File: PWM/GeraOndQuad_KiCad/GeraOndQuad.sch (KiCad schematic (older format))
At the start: 54 parts, among them J1 Conn_01x04_Female, J2 Conn_01x02_Female, J3 Conn_01x02_Female, U1 LM324, U2 TL494, U3 LM324, U4 TL494

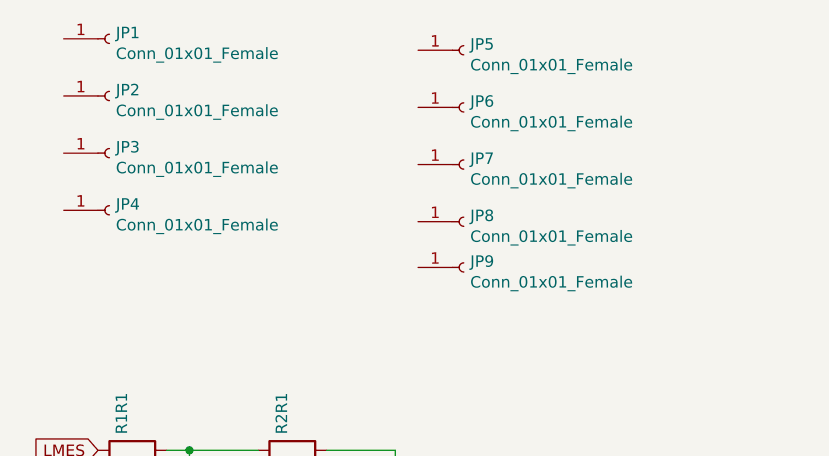
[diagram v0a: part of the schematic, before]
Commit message: corrected kiCad errors
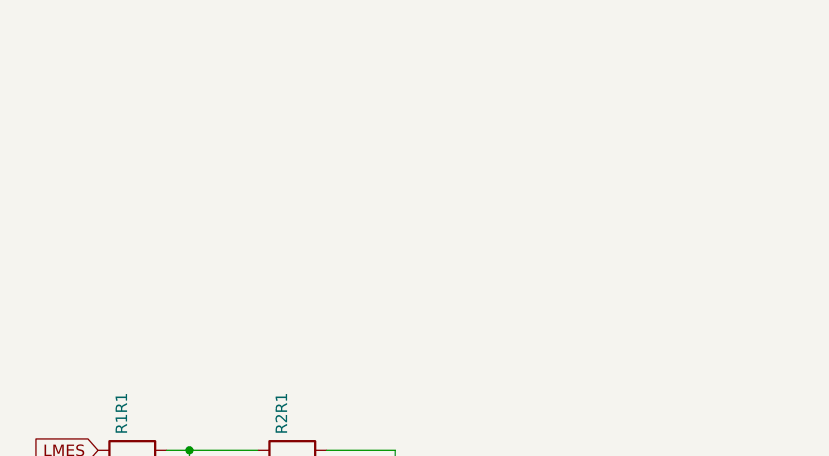
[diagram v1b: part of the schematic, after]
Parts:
- removed JP1, JP2, JP3, JP4, JP5, JP6, JP7, JP8, JP9: Conn_01x01_Female, Connector_Wire:SolderWire-0.5sqmm_1x01_D0.9mm_OD2.1mm, symbol Connector:Conn_01x01_Female
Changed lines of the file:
@@
 	0    1    1    0
 $EndComp
-$Comp
-L Connector:Conn_01x01_Female JP1
-U 1 1 6055F812
-P 950 700
-F 0 "JP1" H 978 726 50  0000 L CNN
-F 1 "Conn_01x01_Female" H 978 635 50  0000 L CNN
-F 2 "Connector_Wire:SolderWire-0.5sqmm_1x01_D0.9mm_OD2.1mm" H 950 700 50  0001 C CNN
-F 3 "~" H 950 700 50  0001 C CNN
-	1    950  700
-	1    0    0    -1
-$EndComp
-$Comp
-L Connector:Conn_01x01_Female JP2
-U 1 1 605605F1
-P 950 950
-F 0 "JP2" H 978 976 50  0000 L CNN
-F 1 "Conn_01x01_Female" H 978 885 50  0000 L CNN
-F 2 "Connector_Wire:SolderWire-0.5sqmm_1x01_D0.9mm_OD2.1mm" H 950 950 50  0001 C CNN
-F 3 "~" H 950 950 50  0001 C CNN
-	1    950  950
-	1    0    0    -1
-$EndComp
-$Comp
-L Connector:Conn_01x01_Female JP3
-U 1 1 605689CD
-P 950 1200
-F 0 "JP3" H 978 1226 50  0000 L CNN
-F 1 "Conn_01x01_Female" H 978 1135 50  0000 L CNN
-F 2 "Connector_Wire:SolderWire-0.5sqmm_1x01_D0.9mm_OD2.1mm" H 950 1200 50  0001 C CNN
-F 3 "~" H 950 1200 50  0001 C CNN
-	1    950  1200
-	1    0    0    -1
-$EndComp
-$Comp
-L Connector:Conn_01x01_Female JP4
-U 1 1 605689D3
-P 950 1450
-F 0 "JP4" H 978 1476 50  0000 L CNN
-F 1 "Conn_01x01_Female" H 978 1385 50  0000 L CNN
-F 2 "Connector_Wire:SolderWire-0.5sqmm_1x01_D0.9mm_OD2.1mm" H 950 1450 50  0001 C CNN
-F 3 "~" H 950 1450 50  0001 C CNN
-	1    950  1450
-	1    0    0    -1
-$EndComp
-$Comp
-L Connector:Conn_01x01_Female JP5
-U 1 1 6063E311
-P 2500 750
-F 0 "JP5" H 2528 776 50  0000 L CNN
-F 1 "Conn_01x01_Female" H 2528 685 50  0000 L CNN
-F 2 "Connector_Wire:SolderWire-0.5sqmm_1x01_D0.9mm_OD2.1mm" H 2500 750 50  0001 C CNN
-F 3 "~" H 2500 750 50  0001 C CNN
-	1    2500 750
-	1    0    0    -1
-$EndComp
-$Comp
-L Connector:Conn_01x01_Female JP6
-U 1 1 6063E317
-P 2500 1000
-F 0 "JP6" H 2528 1026 50  0000 L CNN
-F 1 "Conn_01x01_Female" H 2528 935 50  0000 L CNN
-F 2 "Connector_Wire:SolderWire-0.5sqmm_1x01_D0.9mm_OD2.1mm" H 2500 1000 50  0001 C CNN
-F 3 "~" H 2500 1000 50  0001 C CNN
-	1    2500 1000
-	1    0    0    -1
-$EndComp
-$Comp
-L Connector:Conn_01x01_Female JP7
-U 1 1 6063E31D
-P 2500 1250
-F 0 "JP7" H 2528 1276 50  0000 L CNN
-F 1 "Conn_01x01_Female" H 2528 1185 50  0000 L CNN
-F 2 "Connector_Wire:SolderWire-0.5sqmm_1x01_D0.9mm_OD2.1mm" H 2500 1250 50  0001 C CNN
-F 3 "~" H 2500 1250 50  0001 C CNN
-	1    2500 1250
-	1    0    0    -1
-$EndComp
-$Comp
-L Connector:Conn_01x01_Female JP9
-U 1 1 606452D7
-P 2500 1700
-F 0 "JP9" H 2528 1726 50  0000 L CNN
-F 1 "Conn_01x01_Female" H 2528 1635 50  0000 L CNN
-F 2 "Connector_Wire:SolderWire-0.5sqmm_1x01_D0.9mm_OD2.1mm" H 2500 1700 50  0001 C CNN
-F 3 "~" H 2500 1700 50  0001 C CNN
-	1    2500 1700
-	1    0    0    -1
-$EndComp
-$Comp
-L Connector:Conn_01x01_Female JP8
-U 1 1 6063E323
-P 2500 1500
-F 0 "JP8" H 2528 1526 50  0000 L CNN
-F 1 "Conn_01x01_Female" H 2528 1435 50  0000 L CNN
-F 2 "Connector_Wire:SolderWire-0.5sqmm_1x01_D0.9mm_OD2.1mm" H 2500 1500 50  0001 C CNN
-F 3 "~" H 2500 1500 50  0001 C CNN
-	1    2500 1500
-	1    0    0    -1
-$EndComp
 $EndSCHEMATC
